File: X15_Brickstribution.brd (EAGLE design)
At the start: 0 parts

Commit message: git commit -a
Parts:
- added +12V_TEST, +3.3V_TEST, +5V_TEST, 12V_GND_TEST, 3.3V_GND, 48V_GND_TEST, 48V_TEST, 5V_GND, ON/OFF_TEST: (no value), SparkFun-Connectors:1X01
- added BACKPLANE_CONN: IPL1-107-01-X-D-K, X15_Brickstribution:SAMTEC_IPL1-107-01-X-D-K
- added BRICK: BMR480_CONNECTOR, X15_Brickstribution:BMR480_CONNECTOR
- added C1, C2, C3: 0.330mF, X15_Brickstribution:CAP_MZR_JA0_NIP-M
- added CONV_CONN: TSW-110-07-G-S, X15_Brickstribution:CON10_1X10_TU_TSW
- added D1: DIODE-ZENERPZU15B3A,115, SparkFun-DiscreteSemi:SOD-323
- added D10: BLUE, SparkFun-LED:LED-0603
- added D11: WHITE, SparkFun-LED:LED-0603
- added D2: SK34A-TPDO-214AC_HSMA_MCC-M, X15_Brickstribution:DO-214AC_HSMA_MCC-M
- added D3, D4: 19V, SparkFun-DiscreteSemi:SOD-323
- added D5, D6: 250mA/100V, SparkFun-DiscreteSemi:SOD-323
- added D7: 3.6V, SparkFun-DiscreteSemi:SOD-323
- added D8: RED, SparkFun-LED:LED-0603
- added D9: GREEN, SparkFun-LED:LED-0603
- added JP1: JUMPER-SMT_2_NO_SILK_ROUND, SparkFun-Jumpers:SMT-JUMPER_2_NO_SILK_ROUND
- added Q1: 310mA/60V/1.6Ω, SparkFun-DiscreteSemi:SOT323
- added R1, R7: 1M, SparkFun-Resistors:0603
- added R10: 150, SparkFun-Resistors:0603
- added R11: 100, SparkFun-Resistors:0603
- added R2, R3, R4, R5, R6: 10k, SparkFun-Resistors:0603
- added R8: 2.49k, SparkFun-Resistors:0603
- added R9: 470, SparkFun-Resistors:0603
- added TETHER_48V, TETHER_GND: 796636-3(TETHER), X15_Brickstribution:CON3_P5MM_VER_TERM-BLK_TYC
- added U$1: IRF1018E_S_SLPBF, X15_Brickstribution:IRF1018E_S_SLPBF
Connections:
- new net +12V: +12V_TEST.1, BRICK.P$7, BRICK.P$8, D2.2, R9.1
- new net +12V_CONV: BACKPLANE_CONN.07, CONV_CONN.1, CONV_CONN.2, D2.1
- new net +3.3V: +3.3V_TEST.1, BACKPLANE_CONN.04, CONV_CONN.7, CONV_CONN.8, R11.1, R2.2, R3.2, R4.2, R5.2
- new net +48V: 48V_TEST.1, BRICK.P$1, C1.2, C2.2, C3.2, D4.C, D5.C, R1.2, R6.2, R8.1, TETHER_48V.1, TETHER_48V.2, TETHER_48V.3
- new net +5V: +5V_TEST.1, BACKPLANE_CONN.01, BACKPLANE_CONN.02, BACKPLANE_CONN.03, CONV_CONN.5, CONV_CONN.6, R10.1
- new net 12V_GND: 12V_GND_TEST.1, BACKPLANE_CONN.14, BRICK.P$4, BRICK.P$5, CONV_CONN.3, CONV_CONN.4, D9.C
- new net 48V_GND: 48V_GND_TEST.1, BRICK.P$3, C1.1, C2.1, C3.1, D1.A, D7.A, D8.C, JP1.1, Q1.2, R7.1, U$1.P$3
- new net ALERT_1: BACKPLANE_CONN.09, R3.1
- new net ALERT_2: BACKPLANE_CONN.10, R4.1
- new net C2_1: BACKPLANE_CONN.12
- new net C2_2: BACKPLANE_CONN.13
- new net CLK: BACKPLANE_CONN.11, R5.1
- new net DATA: BACKPLANE_CONN.08, R2.1
- new net D_GND: 3.3V_GND.1, 5V_GND.1, BACKPLANE_CONN.05, BACKPLANE_CONN.06, CONV_CONN.10, CONV_CONN.9, D10.C, D11.C
- new net GND_RAW: TETHER_GND.1, TETHER_GND.2, TETHER_GND.3, U$1.P$2
- new net N$1: D1.C, R1.1, U$1.P$1
- new net N$10: D11.A, R11.2
- new net N$2: BRICK.P$2
- new net N$4: D8.A, R8.2
- new net N$5: D3.C, D4.A
- new net N$6: D3.A, D6.A, R7.2
- new net N$7: D5.A, D6.C, Q1.1
- new net N$8: D9.A, R9.2
- new net N$9: D10.A, R10.2
- new net ON/OFF: D7.C, JP1.2, ON/OFF_TEST.1, Q1.3, R6.1

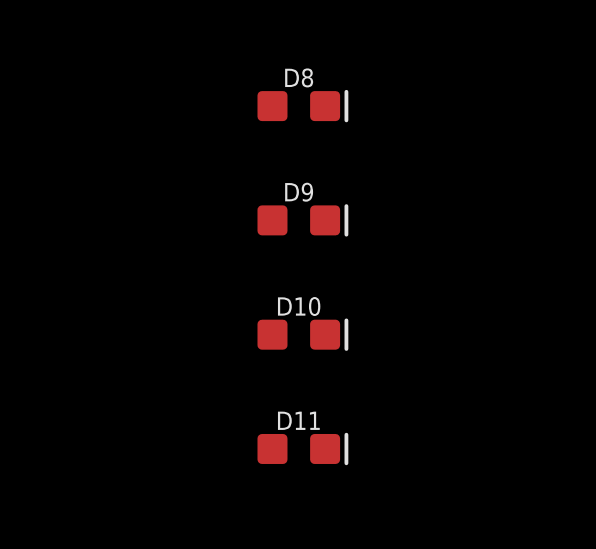
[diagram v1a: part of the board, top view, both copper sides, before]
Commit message: Schematic V1 - Added Backplane Connections
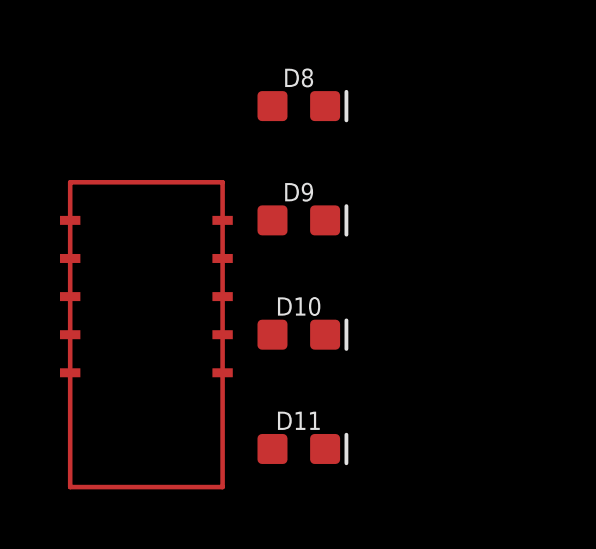
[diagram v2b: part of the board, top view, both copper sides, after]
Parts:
- added BACKPLANE_POWER: CONN_MPPT-10-01-01-L-RA-SD, X15_Brickstribution:MPPT-10-01-01-L-RA-SD(PLACEHOLDER)
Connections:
- net +12V_CONV: now also BACKPLANE_POWER.2, BACKPLANE_POWER.3, BACKPLANE_POWER.4, BACKPLANE_POWER.5, BACKPLANE_POWER.6
- net 12V_GND: now also BACKPLANE_POWER.10, BACKPLANE_POWER.11, BACKPLANE_POWER.7, BACKPLANE_POWER.8, BACKPLANE_POWER.9
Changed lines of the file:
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@@
 <attribute name="VALUE" x="-81.28" y="-361.315" size="0.6096" layer="27" font="vector" ratio="20" align="top-center"/>
 </element>
+<element name="BACKPLANE_POWER" library="X15_Brickstribution" package="MPPT-10-01-01-L-RA-SD(PLACEHOLDER)" value="CONN_MPPT-10-01-01-L-RA-SD" x="-86.36" y="-356.87" smashed="yes"/>
 </elements>
 <signals>
@@
 <contactref element="CONV_CONN" pad="4"/>
 <contactref element="D9" pad="C"/>
+<contactref element="BACKPLANE_POWER" pad="7"/>
+<contactref element="BACKPLANE_POWER" pad="9"/>
+<contactref element="BACKPLANE_POWER" pad="8"/>
+<contactref element="BACKPLANE_POWER" pad="10"/>
+<contactref element="BACKPLANE_POWER" pad="11"/>
 <wire x1="-25.4" y1="-210.82" x2="-27.94" y2="-210.82" width="0" layer="19" extent="1-1"/>
 <wire x1="-35.56" y1="-154.94" x2="-27.94" y2="-210.82" width="0" layer="19" extent="1-1"/>
@@
 <wire x1="43.43" y1="-43.33" x2="43.43" y2="-47.14" width="0" layer="19" extent="1-1"/>
 <wire x1="-80.403" y1="-353.06" x2="-27.94" y2="-210.82" width="0" layer="19" extent="1-1"/>
+<wire x1="-83.82" y1="-353.06" x2="-80.403" y2="-353.06" width="0" layer="19" extent="1-1"/>
+<wire x1="-83.82" y1="-354.33" x2="-83.82" y2="-353.06" width="0" layer="19" extent="1-1"/>
+<wire x1="-83.82" y1="-355.6" x2="-83.82" y2="-354.33" width="0" layer="19" extent="1-1"/>
+<wire x1="-83.82" y1="-356.87" x2="-83.82" y2="-355.6" width="0" layer="19" extent="1-1"/>
+<wire x1="-83.82" y1="-358.14" x2="-83.82" y2="-356.87" width="0" layer="19" extent="1-1"/>
 </signal>
 <signal name="+12V">
@@
 <contactref element="CONV_CONN" pad="1"/>
 <contactref element="CONV_CONN" pad="2"/>
+<contactref element="BACKPLANE_POWER" pad="2"/>
+<contactref element="BACKPLANE_POWER" pad="3"/>
+<contactref element="BACKPLANE_POWER" pad="4"/>
+<contactref element="BACKPLANE_POWER" pad="5"/>
+<contactref element="BACKPLANE_POWER" pad="6"/>
 <wire x1="-30.48" y1="-210.82" x2="-33.02" y2="-210.82" width="0" layer="19" extent="1-1"/>
 <wire x1="-40.4713" y1="-167.64" x2="-33.02" y2="-210.82" width="0" layer="19" extent="1-1"/>
 <wire x1="-35.56" y1="-152.4" x2="-40.4713" y2="-167.64" width="0" layer="19" extent="1-1"/>
+<wire x1="-88.9" y1="-353.06" x2="-33.02" y2="-210.82" width="0" layer="19" extent="1-1"/>
+<wire x1="-88.9" y1="-354.33" x2="-88.9" y2="-353.06" width="0" layer="19" extent="1-1"/>
+<wire x1="-88.9" y1="-355.6" x2="-88.9" y2="-354.33" width="0" layer="19" extent="1-1"/>
+<wire x1="-88.9" y1="-356.87" x2="-88.9" y2="-355.6" width="0" layer="19" extent="1-1"/>
+<wire x1="-88.9" y1="-358.14" x2="-88.9" y2="-356.87" width="0" layer="19" extent="1-1"/>
 </signal>
 <signal name="DATA">

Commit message: Schematic Revision V1
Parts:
- added C10, C17, C18, C19, C8, C9: 2.2uF, SparkFun-Capacitors:0603
- added C11, C20: 1000uF, X15_Brickstribution:CAP_PC_10X12P7_NCH-M
- added C12, C21: 1.0uF, SparkFun-Capacitors:0603
- added C13, C4: 0.22uF, SparkFun-Capacitors:0603
- added C14, C5: 2.2nF, SparkFun-Capacitors:0603
- added C15, C6: 390pF, SparkFun-Capacitors:0603
- added C16, C7: 22nF, SparkFun-Capacitors:0603
- added R12, R16: 15k, SparkFun-Resistors:0603
- added R13, R17: 16k, SparkFun-Resistors:0603
- added R14, R18: 10k, SparkFun-Resistors:0603
- added R15, R19: 20k, SparkFun-Resistors:0603
- added R20: DIODE_RBQ30NS45AFHTLTRANS_R5009FNJ_ROM-M, X15_Brickstribution:TRANS_R5009FNJ_ROM-M
- added U$2, U$3: 40uH, X15_Brickstribution:TRANS_PG1096_26X26_PUL-M
- added U$4: CONN_MPPT-10-01-01-L-RA-SD, X15_Brickstribution:MPPT-10-01-01-L-RA-SD(PLACEHOLDER)
- added U1, U2: IC_L4970A, X15_Brickstribution:MULTIWATT15_V_STM
- added U3, U4: DIODE_STPS1545CT, X15_Brickstribution:TO-220AB_STM
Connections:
- new net +7.4V_SERVO: R20.1, U$4.2, U$4.3, U$4.4, U$4.5, U$4.6
- new net N$11: C7.1, R12.2
- new net N$14: C13.1, C4.1, U1.6, U2.6
- new net N$15: C14.2, C5.2, U1.2, U2.2
- new net N$16: C15.2, C16.2, C6.2, C7.2, U1.10, U2.10
- new net N$17: R13.2, R17.2, U1.1, U2.1
- new net N$18: C17.2, C8.2, U1.12, U2.12
- new net N$20: C18.2, C9.2, U1.14, U2.14
- new net N$22: C13.2, C4.2, U$2.2, U$3.2, U1.7, U2.7, U3.2, U4.2
- new net N$24: C10.2, C19.2, U1.15, U2.15
- new net N$3: C16.1, R16.2
- new net NC: U1.13, U1.4, U1.5, U2.13, U2.4, U2.5
- new net VOUT1: C11.1, C12.2, R14.2, R20.3, U$2.1
- new net VOUT2: C20.1, C21.2, R18.2, R20.2, U$3.1
- new net VREF1: R14.1, R15.2, U1.11
- new net VREF2: R18.1, R19.2, U2.11
- net +12V_CONV: now also U1.9, U2.9
- net 12V_GND: now also C10.1, C11.2, C12.1, C14.1, C15.1, C17.1, C18.1, C19.1, C20.2, C21.1, C5.1, C6.1, C8.1, C9.1, R12.1, R13.1, R15.1, R16.1, R17.1, R19.1, U$4.10, U$4.11, U$4.7, U$4.8, U$4.9, U1.3, U1.8, U2.3, U2.8, U3.1, U3.3, U4.1, U4.3

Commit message: Cleaned all backup files and updated schematic for revisions v1
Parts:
- removed BRICK: BMR480_CONNECTOR, X15_Brickstribution:BMR480_CONNECTOR
- removed C10, C17, C18, C19, C8, C9: 2.2uF, SparkFun-Capacitors:0603
- removed C11, C20: 1000uF, X15_Brickstribution:CAP_PC_10X12P7_NCH-M
- removed C12, C21: 1.0uF, SparkFun-Capacitors:0603
- removed C13, C4: 0.22uF, SparkFun-Capacitors:0603
- removed C14, C5: 2.2nF, SparkFun-Capacitors:0603
- removed C15, C6: 390pF, SparkFun-Capacitors:0603
- removed C16, C7: 22nF, SparkFun-Capacitors:0603
- removed R12, R16: 15k, SparkFun-Resistors:0603
- removed R13, R17: 16k, SparkFun-Resistors:0603
- removed R14, R18: 10k, SparkFun-Resistors:0603
- removed R15, R19: 20k, SparkFun-Resistors:0603
- removed R20: DIODE_RBQ30NS45AFHTLTRANS_R5009FNJ_ROM-M, X15_Brickstribution:TRANS_R5009FNJ_ROM-M
- removed U$3: 40uH, X15_Brickstribution:TRANS_PG1096_26X26_PUL-M
- removed U$4: CONN_MPPT-10-01-01-L-RA-SD, X15_Brickstribution:MPPT-10-01-01-L-RA-SD(PLACEHOLDER)
- removed U1, U2: IC_L4970A, X15_Brickstribution:MULTIWATT15_V_STM
- removed U3, U4: DIODE_STPS1545CT, X15_Brickstribution:TO-220AB_STM
- added +7.4VOUT1_TEST, +7.4VOUT2_TEST, +7.4V_SERVO_TEST, 7.4V_GND: (no value), SparkFun-Connectors:1X01
- added C22, C31: 0.22uF, SparkFun-Capacitors:0603
- added C23, C32: 2.2nF, SparkFun-Capacitors:0603
- added C24, C33: 390pF, SparkFun-Capacitors:0603
- added C25, C34: 22nF, SparkFun-Capacitors:0603
- added C26, C27, C28, C35, C36, C37: 2.2uF, SparkFun-Capacitors:0603
- added C29, C38: 1000uF, X15_Brickstribution:CAP_PC_10X12P7_NCH-M
- added C30, C39: 1.0uF, SparkFun-Capacitors:0603
- added D12, D13: GREEN, SparkFun-LED:LED-0603
- added R21, R22: 470, SparkFun-Resistors:0603
- added R23, R27: 15k, SparkFun-Resistors:0603
- added R24, R28: 16k, SparkFun-Resistors:0603
- added R25, R29: 10k, SparkFun-Resistors:0603
- added R26, R30: 20k, SparkFun-Resistors:0603
- added R31: DIODE_RBQ30NS45AFHTLTRANS_R5009FNJ_ROM-M, X15_Brickstribution:TRANS_R5009FNJ_ROM-M
- added U$5, U$6: 40uH, X15_Brickstribution:TRANS_PG1096_26X26_PUL-M
- added U$7: CONN_MPPT-10-01-01-L-RA-SD, X15_Brickstribution:MPPT-10-01-01-L-RA-SD(PLACEHOLDER)
- added U5, U7: IC_L4970A, X15_Brickstribution:MULTIWATT15_V_STM
- added U6, U8: DIODE_STPS1545CT, X15_Brickstribution:TO-220AB_STM
- U$2: value 40uH -> CONN_BMR480_CONNECTOR; device X15_Brickstribution:TRANS_PG1096_26X26_PUL-M -> X15_Brickstribution:BMR480_CONNECTOR
- moved U$2 482.5 mm to (-100.3, -859.8)
- moved BACKPLANE_POWER 456.1 mm to (-99.1, -812.8)
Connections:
- removed net N$11: C7.1, R12.2
- removed net N$16: C15.2, C16.2, C6.2, C7.2, U1.10, U2.10
- removed net N$17: R13.2, R17.2, U1.1, U2.1
- removed net N$18: C17.2, C8.2, U1.12, U2.12
- removed net N$20: C18.2, C9.2, U1.14, U2.14
- removed net N$22: C13.2, C4.2, U$2.2, U$3.2, U1.7, U2.7, U3.2, U4.2
- removed net N$24: C10.2, C19.2, U1.15, U2.15
- new net BOOT2: C31.1, U7.6
- new net BOOT_1: C22.1, U5.6
- new net C_OSC1: C23.2, U5.2
- new net C_OSC2: C32.2, U7.2
- new net FCOMP1: C24.2, C25.2, U5.10
- new net FCOMP2: C33.2, C34.2, U7.10
- new net N$12: D12.A, R21.2
- new net N$13: D13.A, R22.2
- new net OUT1: C22.2, U$5.2, U5.7, U6.2
- new net OUT2: C31.2, U$6.2, U7.7, U8.2
- new net R_OSC1: R24.2, U5.1
- new net R_OSC2: R28.2, U7.1
- new net SS1: C26.2, U5.12
- new net SS2: C35.2, U7.12
- new net VSTART1: C28.2, U5.15
- new net VSTART2: C37.2, U7.15
- new net V_REF_CAP1: C27.2, U5.14
- new net V_REF_CAP2: C36.2, U7.14
- net +12V: now also R22.1, U$2.PIN8; no longer BRICK.P$7, BRICK.P$8
- net +12V_CONV: now also U5.9, U7.9; no longer U1.9, U2.9
- net +48V: now also U$2.PIN1; no longer BRICK.P$1
- net +7.4V_SERVO: now also +7.4V_SERVO_TEST.1, R31.1, U$7.2, U$7.3, U$7.4, U$7.5, U$7.6; no longer R20.1, U$4.2, U$4.3, U$4.4, U$4.5, U$4.6
- net 12V_GND: now also C23.1, C24.1, C26.1, C27.1, C28.1, C29.2, C30.1, C32.1, C33.1, C35.1, C36.1, C37.1, C38.2, C39.1, D12.C, D13.C, R23.1, R24.1, R26.1, R27.1, R28.1, R30.1, U$2.PIN5, U$7.10, U$7.11, U$7.7, U$7.8, U$7.9, U5.3, U5.8, U6.1, U6.3, U7.3, U7.8, U8.1, U8.3; no longer BRICK.P$4, BRICK.P$5, C10.1, C11.2, C12.1, C14.1, C15.1, C17.1, C18.1, C19.1, C20.2, C21.1, C5.1, C6.1, C8.1, C9.1, R12.1, R13.1, R15.1, R16.1, R17.1, R19.1, U$4.10, U$4.11, U$4.7, U$4.8, U$4.9, U1.3, U1.8, U2.3, U2.8, U3.1, U3.3, U4.1, U4.3
- net 48V_GND: now also U$2.PIN3; no longer BRICK.P$3
- net D_GND: now also 7.4V_GND.1
- net N$14: now also C25.1, R23.2; no longer C13.1, C4.1, U1.6, U2.6
- net N$15: now also C34.1, R27.2; no longer C14.2, C5.2, U1.2, U2.2
- net N$2: now also U$2.PIN4; no longer BRICK.P$2
- net N$3: now also U$2.PIN7; no longer C16.1, R16.2
- net NC: now also U$2.PIN2, U5.13, U5.4, U5.5, U7.13, U7.4, U7.5; no longer U1.13, U1.4, U1.5, U2.13, U2.4, U2.5
- net VOUT1: now also +7.4VOUT1_TEST.1, C29.1, C30.2, R21.1, R25.2, R31.3, U$5.1; no longer C11.1, C12.2, R14.2, R20.3, U$2.1
- net VOUT2: now also +7.4VOUT2_TEST.1, C38.1, C39.2, R29.2, R31.2, U$6.1; no longer C20.1, C21.2, R18.2, R20.2, U$3.1
- net VREF1: now also R25.1, R26.2, U5.11; no longer R14.1, R15.2, U1.11
- net VREF2: now also R29.1, R30.2, U7.11; no longer R18.1, R19.2, U2.11

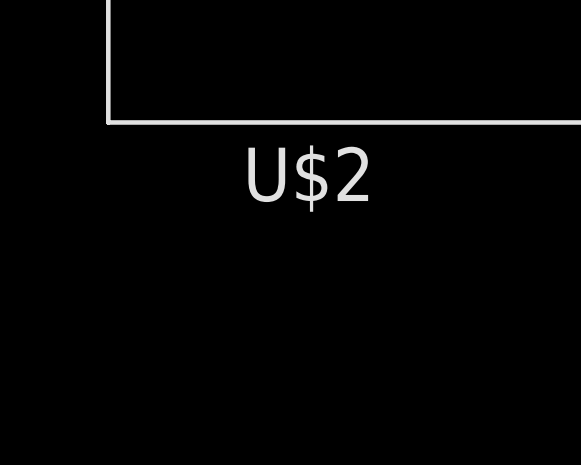
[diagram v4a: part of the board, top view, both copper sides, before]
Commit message: Revision V3 Schematic - LED's added for current source
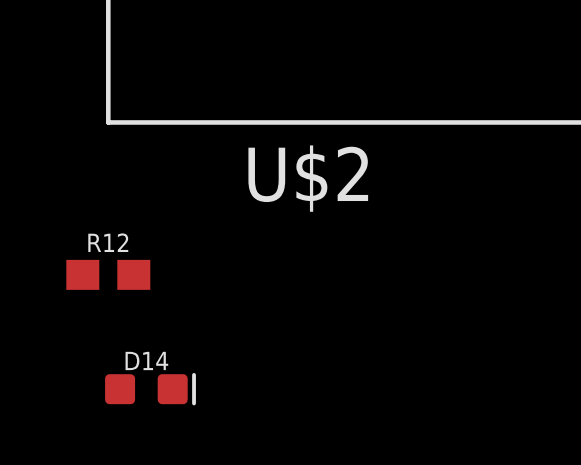
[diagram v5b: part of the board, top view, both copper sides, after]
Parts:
- added D14: RED, SparkFun-LED:LED-0603
- added R12: 470, SparkFun-Resistors:0603
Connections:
- new net N$11: D14.A, R12.2
- net 12V_GND: now also D14.C
- net VOUT2: now also R12.1
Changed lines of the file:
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@@
 <attribute name="VALUE" x="-100.71" y="-821.48" size="1.778" layer="27"/>
+</element>
+<element name="R12" library="SparkFun-Resistors" library_urn="urn:adsk.eagle:library:532" package="0603" package3d_urn="urn:adsk.eagle:package:39650/1" value="470" x="-100.33" y="-864.87" smashed="yes">
+<attribute name="NAME" x="-100.33" y="-864.108" size="0.6096" layer="25" font="vector" ratio="20" align="bottom-center"/>
+<attribute name="PROD_ID" value="RES-07869" x="-99.06" y="-864.87" size="1.778" layer="27" display="off"/>
+<attribute name="VALUE" x="-100.33" y="-865.632" size="0.6096" layer="27" font="vector" ratio="20" align="top-center"/>
+</element>
+<element name="D14" library="SparkFun-LED" library_urn="urn:adsk.eagle:library:529" package="LED-0603" package3d_urn="urn:adsk.eagle:package:39354/1" value="RED" x="-99.06" y="-868.68" smashed="yes">
+<attribute name="NAME" x="-99.06" y="-868.045" size="0.6096" layer="25" font="vector" ratio="20" align="bottom-center"/>
+<attribute name="PROD_ID" value="DIO-00819" x="-99.06" y="-868.68" size="1.778" layer="27" display="off"/>
+<attribute name="VALUE" x="-99.06" y="-869.315" size="0.6096" layer="27" font="vector" ratio="20" align="top-center"/>
 </element>
 </elements>
@@
 <contactref element="BACKPLANE_POWER" pad="11"/>
 <contactref element="U$2" pad="PIN5"/>
+<contactref element="D14" pad="C"/>
 <wire x1="-93.103" y1="-671.83" x2="-93.103" y2="-664.21" width="0" layer="19" extent="1-1"/>
 <wire x1="-71.900296875" y1="-763.27" x2="-93.103" y2="-671.83" width="0" layer="19" extent="1-1"/>
@@
 <wire x1="-45.47" y1="-848.51" x2="-42.76" y2="-810.26" width="0" layer="19" extent="1-1"/>
 <wire x1="-10.940296875" y1="-728.98" x2="-38.1" y2="-762" width="0" layer="19" extent="1-1"/>
+<wire x1="-98.183" y1="-868.68" x2="-96.52" y2="-814.07" width="0" layer="19" extent="1-1"/>
 <wire x1="-80.403" y1="-353.06" x2="-93.103" y2="-664.21" width="0" layer="19" extent="1-1"/>
 <wire x1="-27.94" y1="-210.82" x2="-80.403" y2="-353.06" width="0" layer="19" extent="1-1"/>
@@
 <contactref element="R29" pad="2"/>
 <contactref element="R31" pad="2"/>
+<contactref element="R12" pad="1"/>
 <wire x1="-39.3922" y1="-681.11" x2="-92.71" y2="-652.78" width="0" layer="19" extent="1-1"/>
 <wire x1="-78.74" y1="-728.0021" x2="-39.3922" y2="-681.11" width="0" layer="19" extent="1-1"/>
@@
 <wire x1="-29.63" y1="-810.26" x2="-80.499703125" y2="-763.27" width="0" layer="19" extent="1-1"/>
 <wire x1="-2.96" y1="-810.26" x2="-29.63" y2="-810.26" width="0" layer="19" extent="1-1"/>
+<wire x1="-101.18" y1="-864.87" x2="-29.63" y2="-810.26" width="0" layer="19" extent="1-1"/>
 </signal>
 <signal name="VOUT1">
@@
 <contactref element="U$2" pad="PIN7"/>
 </signal>
+<signal name="N$11">
+<contactref element="R12" pad="2"/>
+<contactref element="D14" pad="A"/>
+<wire x1="-99.48" y1="-864.87" x2="-99.937" y2="-868.68" width="0" layer="19" extent="1-1"/>
+</signal>
 </signals>
